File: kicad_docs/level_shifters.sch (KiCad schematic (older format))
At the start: 18 parts, among them U2 TL072, U3 TL072

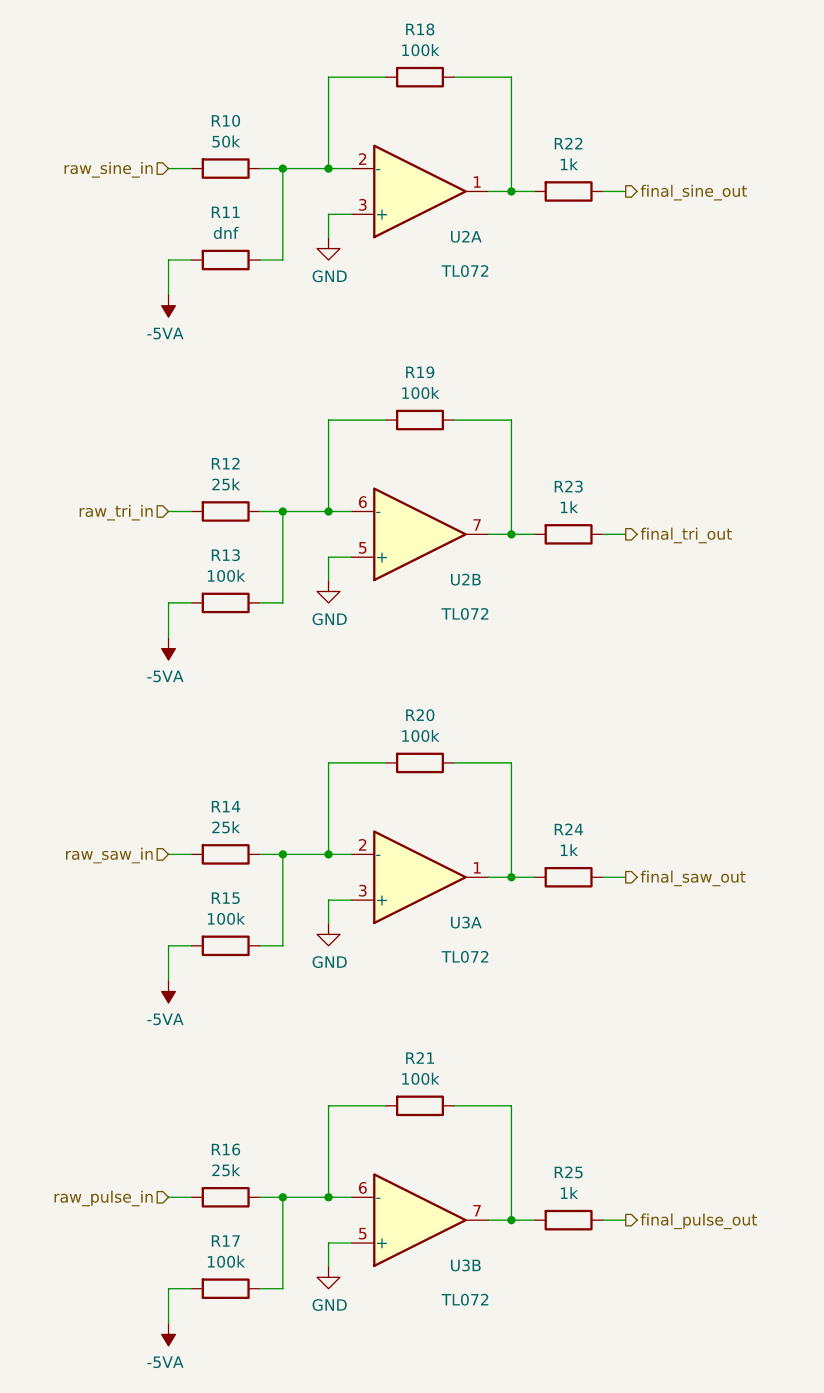
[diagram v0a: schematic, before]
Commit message: reduce amt of weird resistor vals
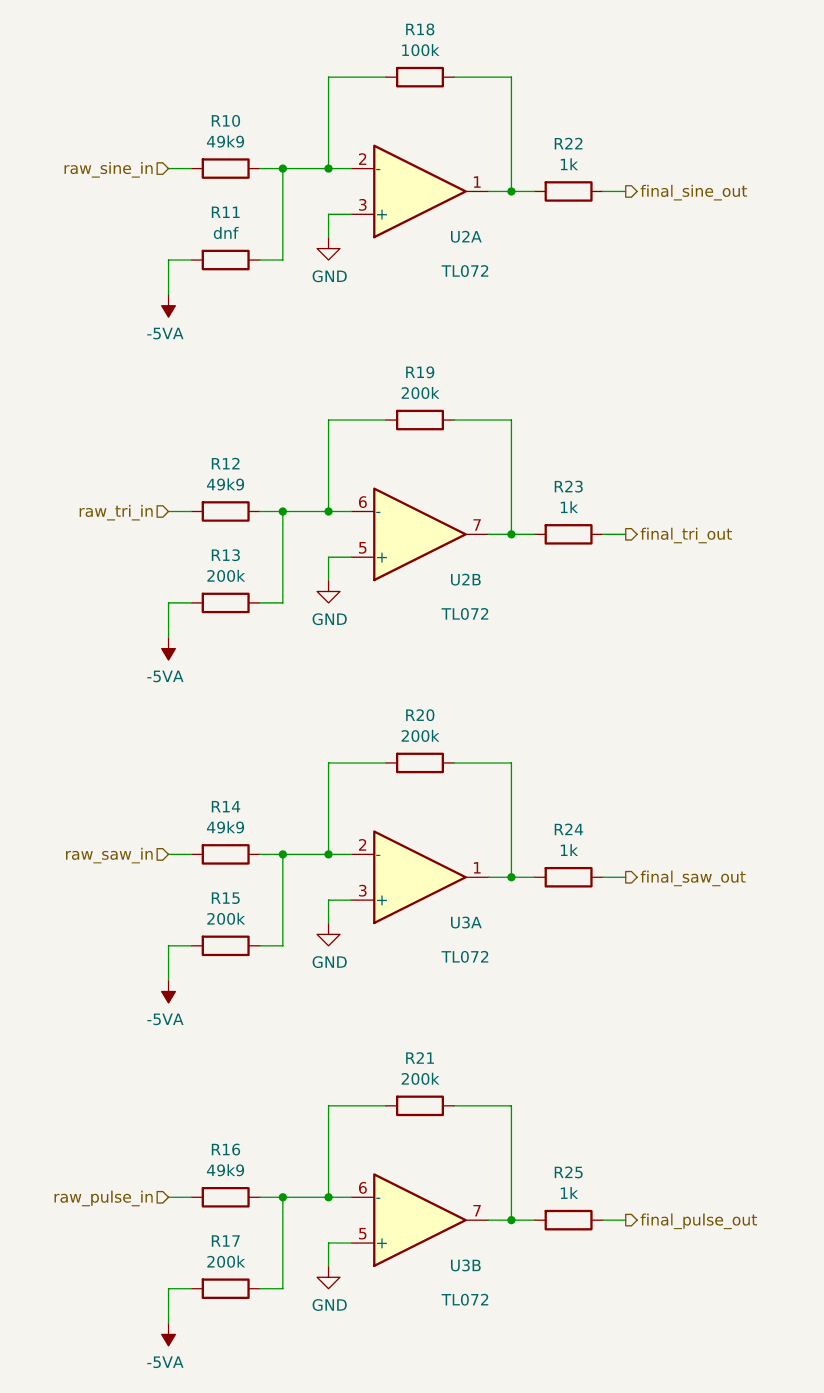
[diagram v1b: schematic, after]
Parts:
- R10: value 50k -> 49k9
- R12, R14, R16: value 25k -> 49k9
- R13, R15, R17, R19, R20, R21: value 100k -> 200k
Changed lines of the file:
@@
 $Descr A4 11693 8268
 encoding utf-8
-Sheet 3 6
+Sheet 5 6
 Title "SSI2130 VCO"
 Date "2021-12-23"
@@
 P 5050 1400
 F 0 "R10" V 4843 1400 50  0000 C CNN
-F 1 "50k" V 4934 1400 50  0000 C CNN
+F 1 "49k9" V 4934 1400 50  0000 C CNN
 F 2 "Resistor_SMD:R_0805_2012Metric" V 4980 1400 50  0001 C CNN
 F 3 "~" H 5050 1400 50  0001 C CNN
@@
 P 5900 2500
 F 0 "R19" V 5693 2500 50  0000 C CNN
-F 1 "100k" V 5784 2500 50  0000 C CNN
+F 1 "200k" V 5784 2500 50  0000 C CNN
 F 2 "Resistor_SMD:R_0805_2012Metric" V 5830 2500 50  0001 C CNN
 F 3 "~" H 5900 2500 50  0001 C CNN
@@
 P 5050 2900
 F 0 "R12" V 4843 2900 50  0000 C CNN
-F 1 "25k" V 4934 2900 50  0000 C CNN
+F 1 "49k9" V 4934 2900 50  0000 C CNN
 F 2 "Resistor_SMD:R_0805_2012Metric" V 4980 2900 50  0001 C CNN
 F 3 "~" H 5050 2900 50  0001 C CNN
@@
 P 5900 4000
 F 0 "R20" V 5693 4000 50  0000 C CNN
-F 1 "100k" V 5784 4000 50  0000 C CNN
+F 1 "200k" V 5784 4000 50  0000 C CNN
 F 2 "Resistor_SMD:R_0805_2012Metric" V 5830 4000 50  0001 C CNN
 F 3 "~" H 5900 4000 50  0001 C CNN
@@
 P 5050 4400
 F 0 "R14" V 4843 4400 50  0000 C CNN
-F 1 "25k" V 4934 4400 50  0000 C CNN
+F 1 "49k9" V 4934 4400 50  0000 C CNN
 F 2 "Resistor_SMD:R_0805_2012Metric" V 4980 4400 50  0001 C CNN
 F 3 "~" H 5050 4400 50  0001 C CNN
@@
 P 5900 5500
 F 0 "R21" V 5693 5500 50  0000 C CNN
-F 1 "100k" V 5784 5500 50  0000 C CNN
+F 1 "200k" V 5784 5500 50  0000 C CNN
 F 2 "Resistor_SMD:R_0805_2012Metric" V 5830 5500 50  0001 C CNN
 F 3 "~" H 5900 5500 50  0001 C CNN
@@
 P 5050 5900
 F 0 "R16" V 4843 5900 50  0000 C CNN
-F 1 "25k" V 4934 5900 50  0000 C CNN
+F 1 "49k9" V 4934 5900 50  0000 C CNN
 F 2 "Resistor_SMD:R_0805_2012Metric" V 4980 5900 50  0001 C CNN
 F 3 "~" H 5050 5900 50  0001 C CNN
@@
 P 5050 3300
 F 0 "R13" V 4843 3300 50  0000 C CNN
-F 1 "100k" V 4934 3300 50  0000 C CNN
+F 1 "200k" V 4934 3300 50  0000 C CNN
 F 2 "Resistor_SMD:R_0805_2012Metric" V 4980 3300 50  0001 C CNN
 F 3 "~" H 5050 3300 50  0001 C CNN
@@
 P 5050 4800
 F 0 "R15" V 4843 4800 50  0000 C CNN
-F 1 "100k" V 4934 4800 50  0000 C CNN
+F 1 "200k" V 4934 4800 50  0000 C CNN
 F 2 "Resistor_SMD:R_0805_2012Metric" V 4980 4800 50  0001 C CNN
 F 3 "~" H 5050 4800 50  0001 C CNN
@@
 P 5050 6300
 F 0 "R17" V 4843 6300 50  0000 C CNN
-F 1 "100k" V 4934 6300 50  0000 C CNN
+F 1 "200k" V 4934 6300 50  0000 C CNN
 F 2 "Resistor_SMD:R_0805_2012Metric" V 4980 6300 50  0001 C CNN
 F 3 "~" H 5050 6300 50  0001 C CNN
